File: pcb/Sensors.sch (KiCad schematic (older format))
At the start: 7 parts, among them U1 MPL3115A2, U13 HTS221

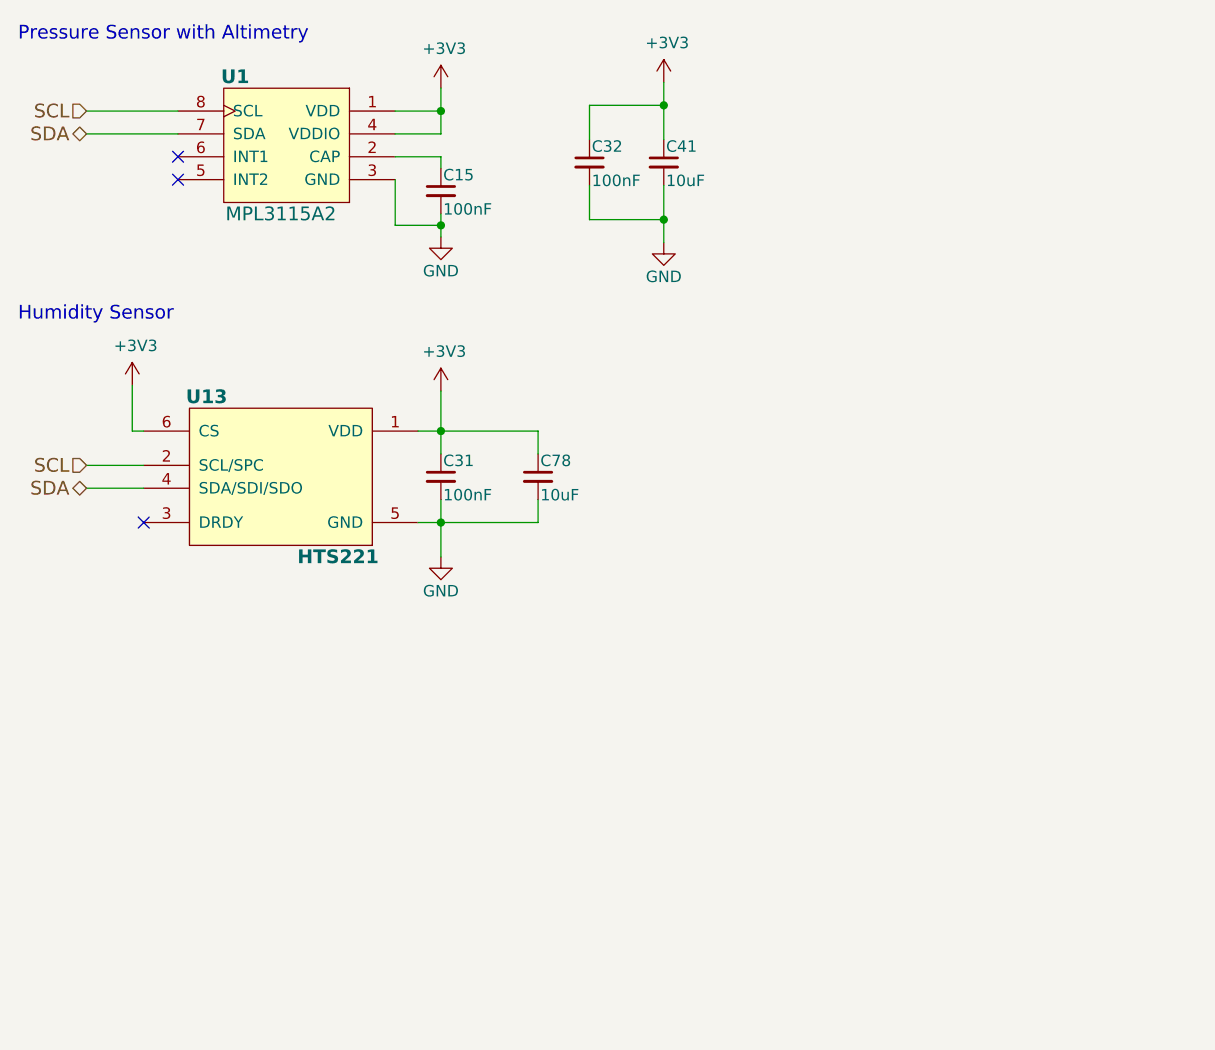
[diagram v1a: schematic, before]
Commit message: fixing missed footprints
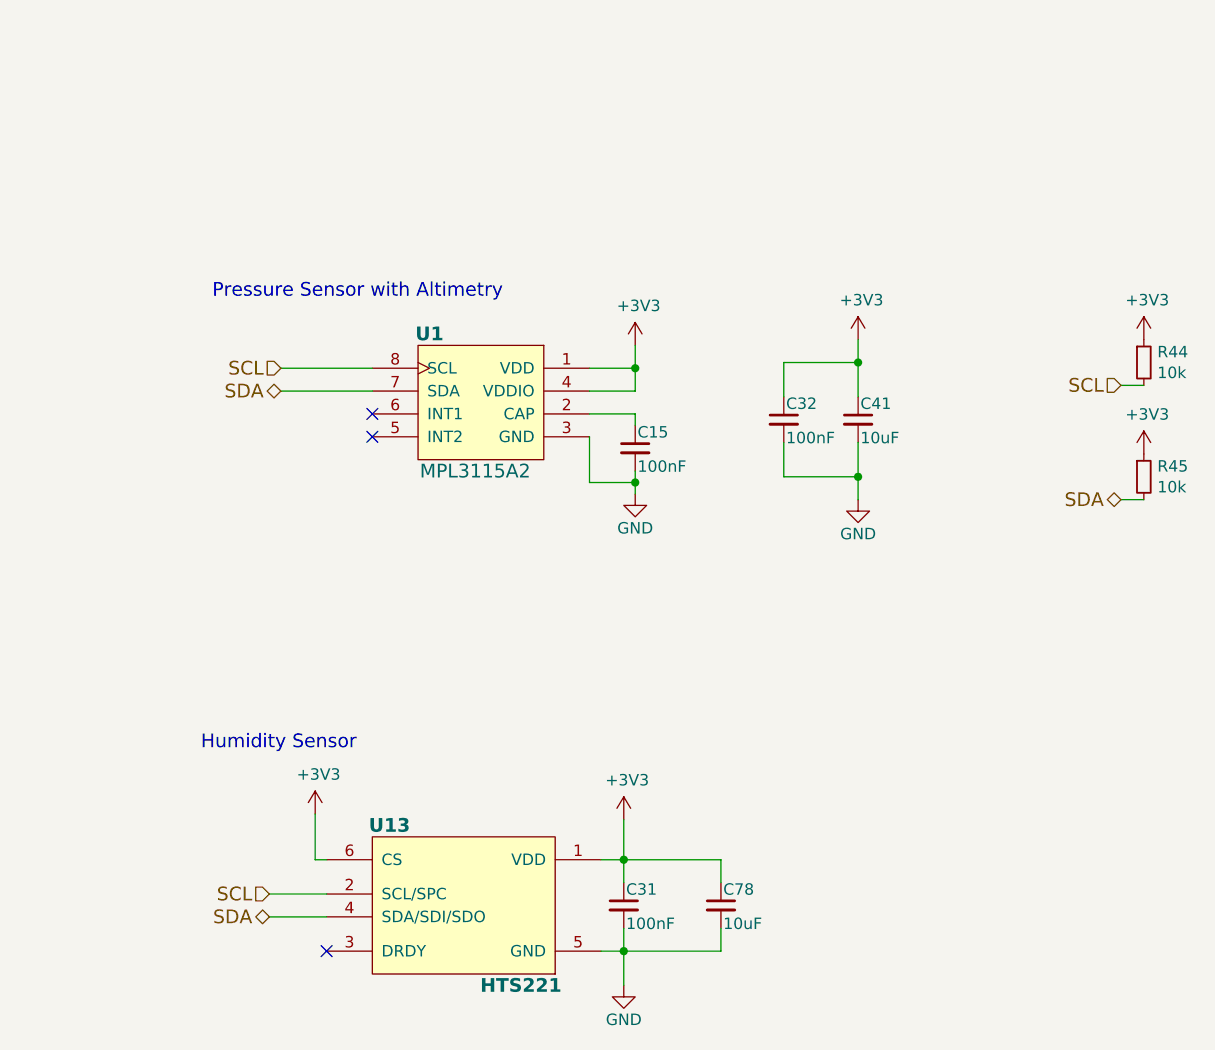
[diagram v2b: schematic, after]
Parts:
- added R44, R45: 10k, Resistor_SMD:R_0402_1005Metric, symbol Device:R_Small
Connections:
- net +3V3: now also R44.1, R45.1
- net SCL: now also R44.2
- net SDA: now also R45.2
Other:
- moved on the sheet: C15, C31, C32, C41, C78, U1, U13
